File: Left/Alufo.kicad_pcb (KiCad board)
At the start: 2 copper layers, 139.7 x 88.9 mm, 67 parts, among them J1 USB_C_Receptacle_USB2.0_16P_2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, J3 USB_C_Receptacle_USB2.0_16P_2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, K11 PG1350, K12 PG1350, K13 PG1350, K14 PG1350, K15 PG1350, K16 PG1350, K21 PG1350, K22 PG1350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

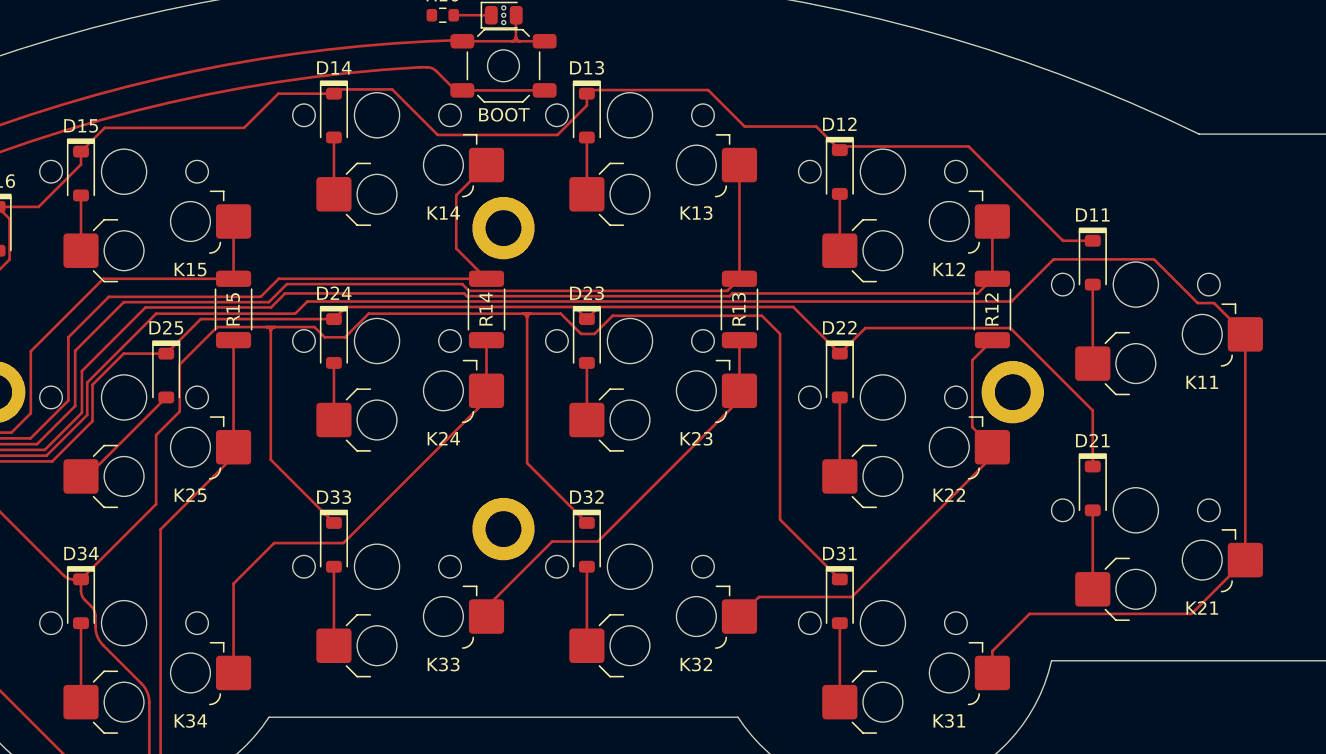
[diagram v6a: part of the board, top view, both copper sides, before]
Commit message: Remove “L” from column labels
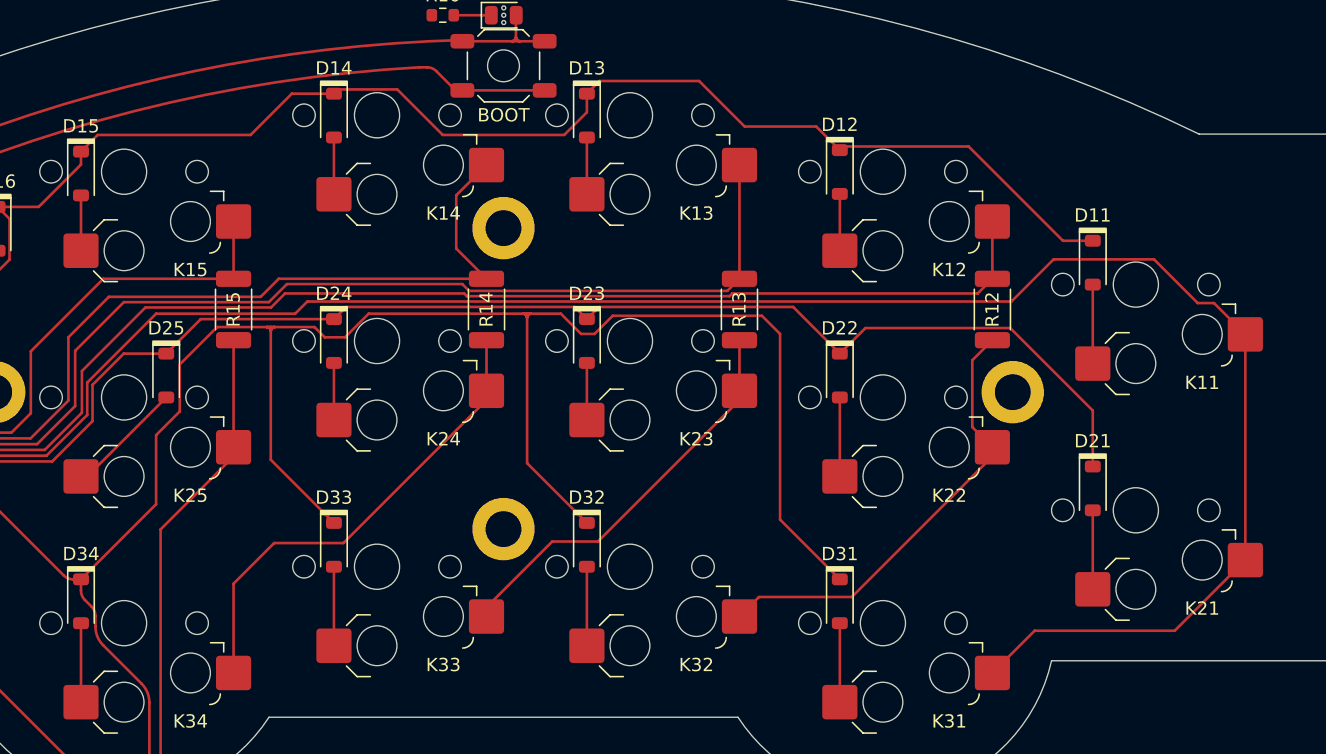
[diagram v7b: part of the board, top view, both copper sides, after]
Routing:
- net Col1: track 173.9 -> 172.9 mm
- net Row1: track 126.5 -> 127.4 mm
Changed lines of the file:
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@@
 	)
 	(segment
-		(start 114.3 46.566677)
-		(end 117.390323 46.566677)
+		(start 133.35 41.148)
+		(end 136.458824 38.039176)
 		(width 0.2)
 		(layer "F.Cu")
@@
 	)
 	(segment
-		(start 104.084 61.905)
-		(end 107.442 58.547)
+		(start 114.3 46.566677)
+		(end 117.390323 46.566677)
 		(width 0.2)
 		(layer "F.Cu")
@@
 	)
 	(segment
+		(start 136.458824 38.039176)
+		(end 139.63 38.039176)
+		(width 0.2)
+		(layer "F.Cu")
+		(net 1)
+	)
+	(segment
+		(start 104.084 61.905)
+		(end 107.442 58.547)
+		(width 0.2)
+		(layer "F.Cu")
+		(net 1)
+	)
+	(segment
 		(start 139.950176 37.719)
-		(end 144.018 37.719)
+		(end 144.399 37.719)
 		(width 0.2)
 		(layer "F.Cu")
@@
 	)
 	(segment
-		(start 147.447 41.148)
-		(end 156.464 41.148)
+		(start 158.9525 37.766676)
+		(end 159.635176 37.084)
 		(width 0.2)
 		(layer "F.Cu")
@@
 	)
 	(segment
-		(start 156.464 41.148)
-		(end 158.68 38.932)
+		(start 159.635176 37.084)
+		(end 167.132 37.084)
 		(width 0.2)
 		(layer "F.Cu")
@@
 	)
 	(segment
-		(start 175.953823 40.513)
-		(end 177.73 42.289177)
+		(start 121.834177 41.148)
+		(end 133.35 41.148)
 		(width 0.2)
 		(layer "F.Cu")
@@
 	)
 	(segment
-		(start 107.442 55.88)
-		(end 108.966 54.356)
+		(start 120.58 42.402177)
+		(end 121.834177 41.148)
 		(width 0.2)
 		(layer "F.Cu")
@@
 	)
 	(segment
-		(start 120.58 42.402177)
-		(end 122.3655 40.616677)
+		(start 107.442 55.88)
+		(end 108.966 54.356)
 		(width 0.2)
 		(layer "F.Cu")
@@
 	)
 	(segment
-		(start 158.9525 37.766676)
-		(end 167.814676 37.766676)
-		(width 0.2)
-		(layer "F.Cu")
-		(net 1)
-	)
-	(segment
-		(start 158.68 38.932)
+		(start 158.68 39.44)
 		(end 158.68 38.039176)
 		(width 0.2)
@@
 	)
 	(segment
-		(start 135.442824 38.039176)
-		(end 139.63 38.039176)
+		(start 175.953823 40.513)
+		(end 177.73 42.289177)
 		(width 0.2)
 		(layer "F.Cu")
@@
 	)
 	(segment
-		(start 115.2 47.466677)
-		(end 114.3 46.566677)
+		(start 156.972 41.148)
+		(end 158.68 39.44)
 		(width 0.2)
 		(layer "F.Cu")
@@
 	)
 	(segment
-		(start 111.379 54.356)
-		(end 115.2 50.535)
+		(start 115.2 47.466677)
+		(end 114.3 46.566677)
 		(width 0.2)
 		(layer "F.Cu")
@@
 	)
 	(segment
-		(start 144.018 37.719)
-		(end 147.447 41.148)
+		(start 111.379 54.356)
+		(end 115.2 50.535)
 		(width 0.2)
 		(layer "F.Cu")
@@
 	)
 	(segment
-		(start 167.814676 37.766676)
-		(end 170.561 40.513)
+		(start 147.828 41.148)
+		(end 156.972 41.148)
 		(width 0.2)
 		(layer "F.Cu")
@@
 	)
 	(segment
-		(start 132.865323 40.616677)
-		(end 135.442824 38.039176)
+		(start 144.399 37.719)
+		(end 147.828 41.148)
 		(width 0.2)
 		(layer "F.Cu")
@@
 	)
 	(segment
-		(start 122.3655 40.616677)
-		(end 132.865323 40.616677)
+		(start 167.132 37.084)
+		(end 170.561 40.513)
 		(width 0.2)
 		(layer "F.Cu")
@@
 	)
 	(segment
-		(start 137.628007 53.691679)
-		(end 190.656321 53.691679)
+		(start 202.950683 78.486)
+		(end 192.400685 78.486)
 		(width 0.2)
 		(layer "F.Cu")
@@
 	)
 	(segment
-		(start 90.459448 65.067005)
-		(end 90.525076 65.180686)
-		(width 0.2)
-		(layer "F.Cu")
-		(net 58)
-	)
-	(segment
-		(start 204.220683 77.216)
-		(end 192.024 77.216)
+		(start 137.628007 53.691679)
+		(end 190.656321 53.691679)
 		(width 0.2)
 		(layer "F.Cu")
@@
 	)
 	(segment
-		(start 192.024 77.216)
-		(end 189.22 80.02)
+		(start 90.459448 65.067005)
+		(end 90.525076 65.180686)
 		(width 0.2)
 		(layer "F.Cu")
@@
 	)
 	(segment
+		(start 192.400685 78.486)
+		(end 189.22 81.666685)
+		(width 0.2)
+		(layer "F.Cu")
+		(net 58)
+	)
+	(segment
 		(start 92.205216 66.86048)
 		(end 92.31884 66.926081)
@@
 	)
 	(segment
-		(start 189.22 80.02)
-		(end 189.22 81.666685)
+		(start 121.05 62.235472)
+		(end 121.05 59.798)
 		(width 0.2)
 		(layer "F.Cu")
@@
 	)
 	(segment
-		(start 121.05 62.235472)
-		(end 121.05 59.798)
+		(start 88.165994 62.006083)
+		(end 88.213447 62.051447)
 		(width 0.2)
 		(layer "F.Cu")
@@
 	)
 	(segment
-		(start 88.165994 62.006083)
-		(end 88.213447 62.051447)
+		(start 208.27 73.166683)
+		(end 202.950683 78.486)
 		(width 0.2)
 		(layer "F.Cu")
@@
 		(width 0.2)
 		(layer "F.Cu")
-		(net 58)
-	)
-	(segment
-		(start 208.27 73.166683)
-		(end 204.220683 77.216)
-		(width 0.2)
-		(layer "F.Cu")

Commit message: Remove “L” and “R” from all labels
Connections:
- net Col2L renamed Col2
- net Col3L renamed Col3
- net Col4L renamed Col4
- net Col5L renamed Col5
- net RX_L renamed RX
- net RX_PL renamed RX_P
- net TX_L renamed TX
- net TX_PL renamed TX_P
- net USB_L+ renamed USB+
- net USB_L- renamed USB-
- net USB_PL+ renamed USB_P+
- net USB_PL- renamed USB_P-
- net VBUS_L renamed VBUS
- net VCC_L renamed VCC
- net VCC_L' renamed VCC'
